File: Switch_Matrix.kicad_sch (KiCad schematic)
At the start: 54 parts, among them SW10 MX Hotswap, SW11 MX Hotswap, SW12 MX Hotswap, SW13 MX Hotswap, SW14 MX Hotswap, SW15 MX Hotswap, SW16 MX Hotswap, SW17 MX Hotswap, SW18 MX Hotswap, SW19 MX Hotswap, SW2 MX Hotswap, SW20 MX Hotswap, SW21 MX Hotswap, SW22 MX Hotswap, SW23 MX Hotswap, SW24 MX Hotswap, SW25 MX Hotswap, SW26 MX Hotswap, SW27 MX Hotswap, SW28 MX Hotswap, SW3 MX Hotswap, SW4 MX Hotswap, SW5 MX Hotswap, SW6 MX Hotswap, SW7 MX Hotswap, SW8 MX Hotswap, SW9 MX Hotswap

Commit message: feat(pcb): Version 0.2
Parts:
- D10, D11, D12, D13, D14, D15, D16, D17, D18, D19, D20, D21, D22, D23, D24, D25, D26, D27, D28, D29, D3, D4, D5, D6, D7, D8, D9: value 1N4148 -> (none); footprint Athena54:D_SOD-523 (Reversible) -> (none)
- SW10, SW11, SW12, SW13, SW14, SW15, SW16, SW17, SW18, SW19, SW2, SW20, SW21, SW22, SW23, SW24, SW25, SW26, SW27, SW3, SW4, SW5, SW6, SW7, SW8, SW9: value MX Hotswap -> (none); footprint Athena54:MXOnly-1U-Hotswap-Antishear (reversible) -> (none)
- SW28: value MX Hotswap -> (none); footprint Athena54:MXOnly-1.5U-Hotswap-Antishear (reversible) -> (none)

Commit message: feat(pcb): Version 0.2.1
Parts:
- D10, D11, D12, D13, D14, D15, D16, D17, D18, D19, D20, D21, D22, D23, D24, D25, D26, D27, D28, D29, D3, D4, D5, D6, D7, D8, D9: value (none) -> 1N4148; footprint (none) -> Athena54:D_SOD-523 (Reversible)
- SW10, SW11, SW12, SW13, SW14, SW15, SW16, SW17, SW18, SW19, SW2, SW20, SW21, SW22, SW23, SW24, SW25, SW26, SW27, SW3, SW4, SW5, SW6, SW7, SW8, SW9: value (none) -> MX Hotswap; footprint (none) -> Athena54:MXOnly-1U-Hotswap (Reversible)
- SW28: value (none) -> MX Hotswap; footprint (none) -> Athena54:MXOnly-1.5U-Hotswap (Reversible)

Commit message: refactor!!!(repository): Rename from Athena54 to Conejo
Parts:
- D10, D11, D12, D13, D14, D15, D16, D17, D18, D19, D20, D21, D22, D23, D24, D25, D26, D27, D28, D29, D3, D4, D5, D6, D7, D8, D9: footprint Athena54:D_SOD-523 (Reversible) -> Conejo:D_SOD-523 (Reversible)
- SW10, SW11, SW12, SW13, SW14, SW15, SW16, SW17, SW18, SW19, SW2, SW20, SW21, SW22, SW23, SW24, SW25, SW26, SW27, SW3, SW4, SW5, SW6, SW7, SW8, SW9: footprint Athena54:MXOnly-1U-Hotswap (Reversible) -> Conejo:MXOnly-1U-Hotswap (Reversible)
- SW28: footprint Athena54:MXOnly-1.5U-Hotswap (Reversible) -> Conejo:MXOnly-1.5U-Hotswap (Reversible)

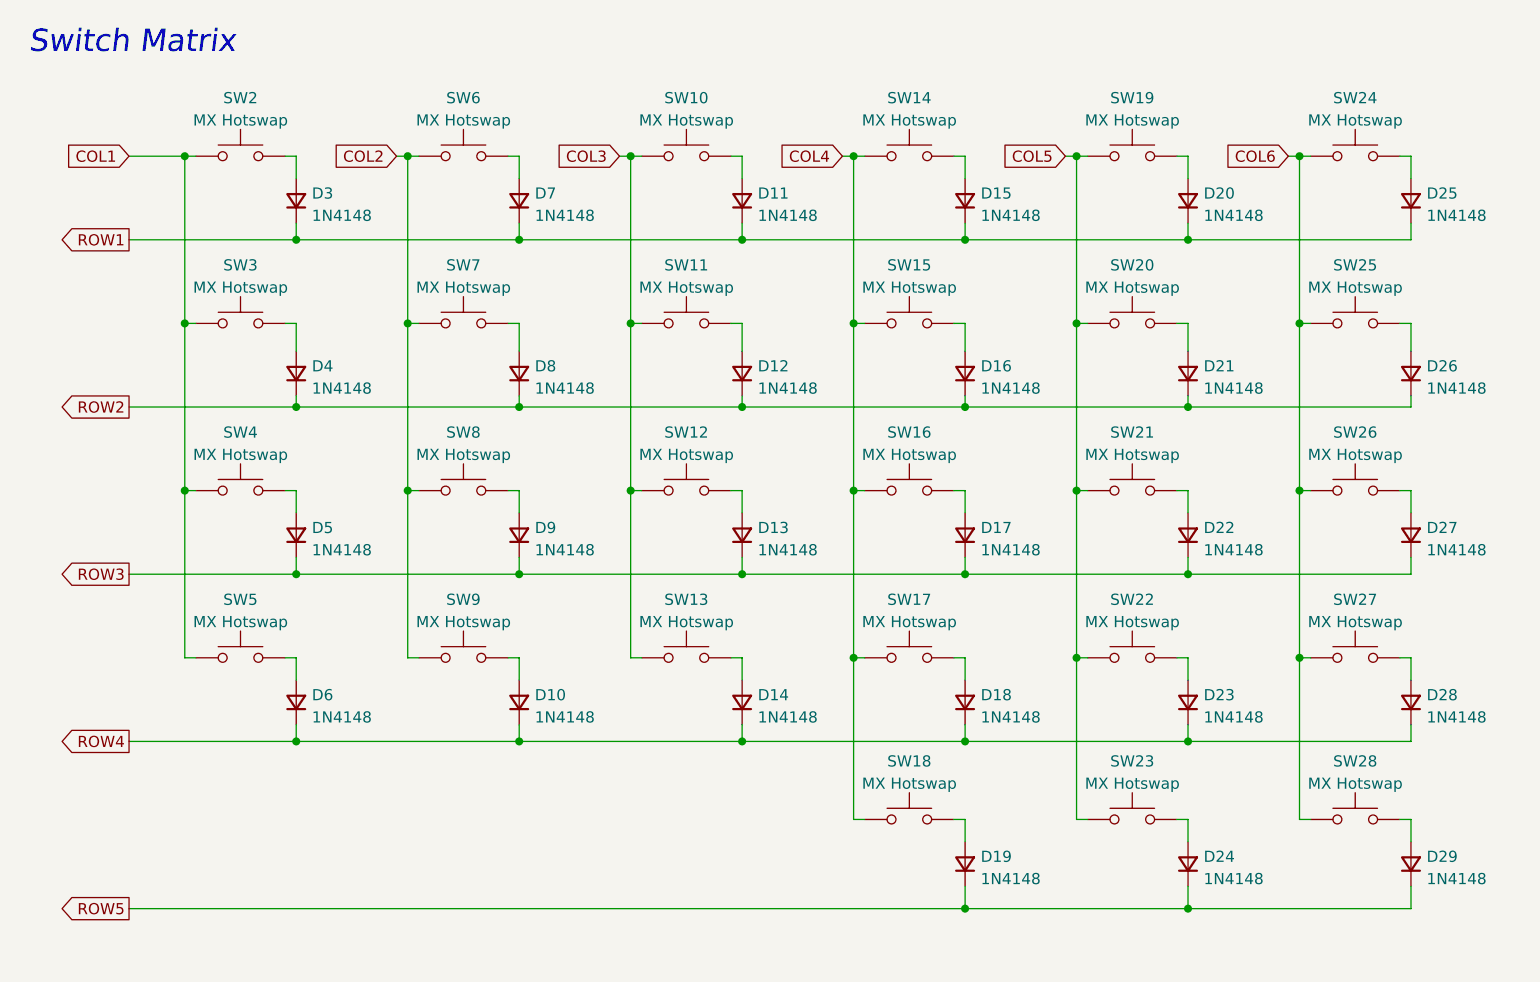
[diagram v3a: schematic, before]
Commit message: feat(schematic): Add titles and individual sheet comments
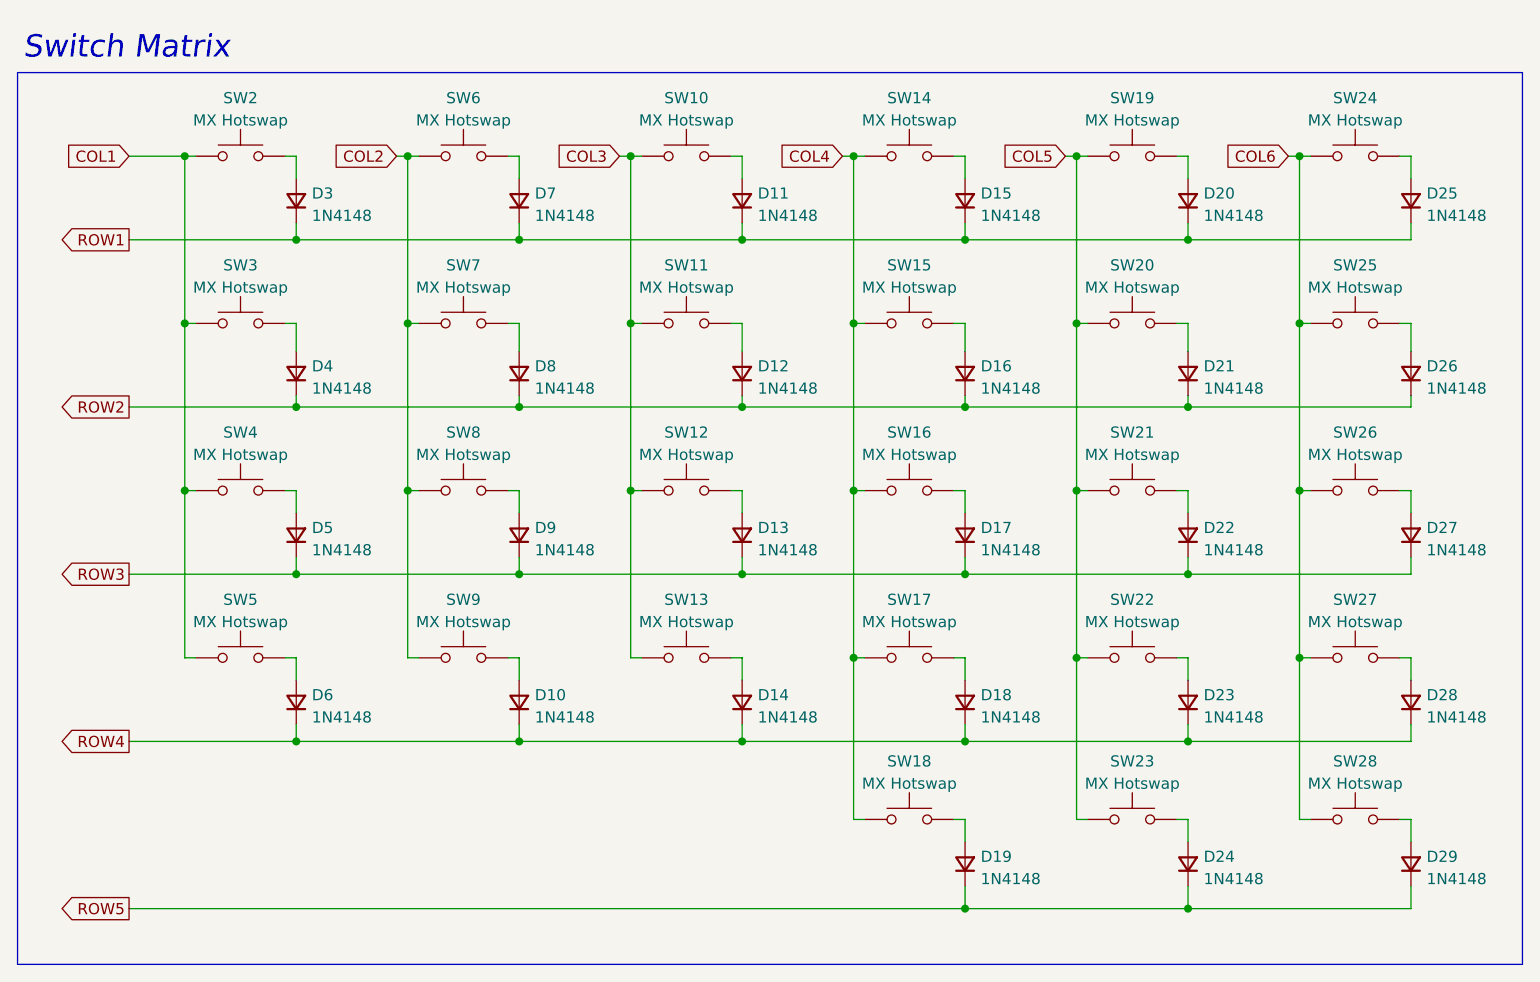
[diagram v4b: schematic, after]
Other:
- company: (none) -> Kurtis Lew
- title: (none) -> Conejo nRF52840 Keyboard - Switch Matrix
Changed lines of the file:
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@@
 (kicad_sch (version 20211123) (generator eeschema)
   (paper "USLetter")
+  (title_block
+    (title "Conejo nRF52840 Keyboard - Switch Matrix")
+    (company "Kurtis Lew")
+  )
   (junction (at 107.95 66.675) (diameter 0) (color 0 0 0 0)
   )
@@
     (stroke (width 0) (type default) (color 0 0 0 0))
   )
+  (polyline (pts (xy 184.15 19.05) (xy 184.15 120.65))
+    (stroke (width 0) (type default) (color 0 0 0 0))
+  )
   (wire (pts (xy 44.45 66.675) (xy 43.18 66.675))
     (stroke (width 0) (type default) (color 0 0 0 0))
@@
     (stroke (width 0) (type default) (color 0 0 0 0))
   )
+  (polyline (pts (xy 184.15 120.65) (xy 12.7 120.65))
+    (stroke (width 0) (type default) (color 0 0 0 0))
+  )
   (wire (pts (xy 31.75 28.575) (xy 31.75 47.625))
     (stroke (width 0) (type default) (color 0 0 0 0))
@@
     (stroke (width 0) (type default) (color 0 0 0 0))
   )
+  (polyline (pts (xy 12.7 19.05) (xy 184.15 19.05))
+    (stroke (width 0) (type default) (color 0 0 0 0))
+  )
   (wire (pts (xy 106.68 28.575) (xy 107.95 28.575))
     (stroke (width 0) (type default) (color 0 0 0 0))
@@
     (stroke (width 0) (type default) (color 0 0 0 0))
   )
+  (polyline (pts (xy 12.7 120.65) (xy 12.7 19.05))
+    (stroke (width 0) (type default) (color 0 0 0 0))
+  )
   (wire (pts (xy 95.25 66.675) (xy 93.98 66.675))
     (stroke (width 0) (type default) (color 0 0 0 0))
@@
     (stroke (width 0) (type default) (color 0 0 0 0))
   )
-  (text "Switch Matrix\n" (at 13.97 17.145 0)
+  (text "Switch Matrix\n" (at 13.335 17.78 0)
     (effects (font (size 2.54 2.54) italic) (justify left bottom))
   )

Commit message: feat(pcb): Switch from 4.3mm NPTH mounting holes to M2 PTH
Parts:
- D10, D11, D12, D13, D14, D15, D16, D17, D18, D19, D20, D21, D22, D23, D24, D25, D26, D27, D28, D29, D3, D4, D5, D6, D7, D8, D9: value 1N4148 -> (none); footprint Conejo:D_SOD-523 (Reversible) -> (none)
- SW10, SW11, SW12, SW13, SW14, SW15, SW16, SW17, SW18, SW19, SW2, SW20, SW21, SW22, SW23, SW24, SW25, SW26, SW27, SW3, SW4, SW5, SW6, SW7, SW8, SW9: value MX Hotswap -> (none); footprint Conejo:MXOnly-1U-Hotswap (Reversible) -> (none)
- SW28: value MX Hotswap -> (none); footprint Conejo:MXOnly-1.5U-Hotswap (Reversible) -> (none)

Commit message: feat(pcb): Version 1.0.0
- Change decoupling capacitors from 4.7uF/1uF pairs to both 4.7uF
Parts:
- D10, D11, D12, D13, D14, D15, D16, D17, D18, D19, D20, D21, D22, D23, D24, D25, D26, D27, D28, D29, D3, D4, D5, D6, D7, D8, D9: value (none) -> 1N4148; footprint (none) -> Conejo:D_SOD-523 (Reversible)
- SW10, SW11, SW12, SW13, SW14, SW15, SW16, SW17, SW18, SW19, SW2, SW20, SW21, SW22, SW23, SW24, SW25, SW26, SW27, SW3, SW4, SW5, SW6, SW7, SW8, SW9: value (none) -> MX Hotswap; footprint (none) -> Conejo:MXOnly-1U-Hotswap (Reversible)
- SW28: value (none) -> MX Hotswap; footprint (none) -> Conejo:MXOnly-1.5U-Hotswap (Reversible)
